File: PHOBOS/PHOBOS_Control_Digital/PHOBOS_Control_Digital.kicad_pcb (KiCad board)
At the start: 4 copper layers, 58.4 x 35.6 mm, 71 parts, among them J12 PWR, J14 PS1-2, J15 PS3-4, J2 RF_OUT, J3 USB4056-03-A_REVA2, J4 BATT, J8 BOOT, U1 SX1280IMLTRT, U2 W25Q128JVSIQ, U3 NCP1117-3.3_SOT223, U4 RP2040, U5 TPS60403DBV, Y1 C1E-52.000-10-1012-X-M, Y2 ABM8-272-T3

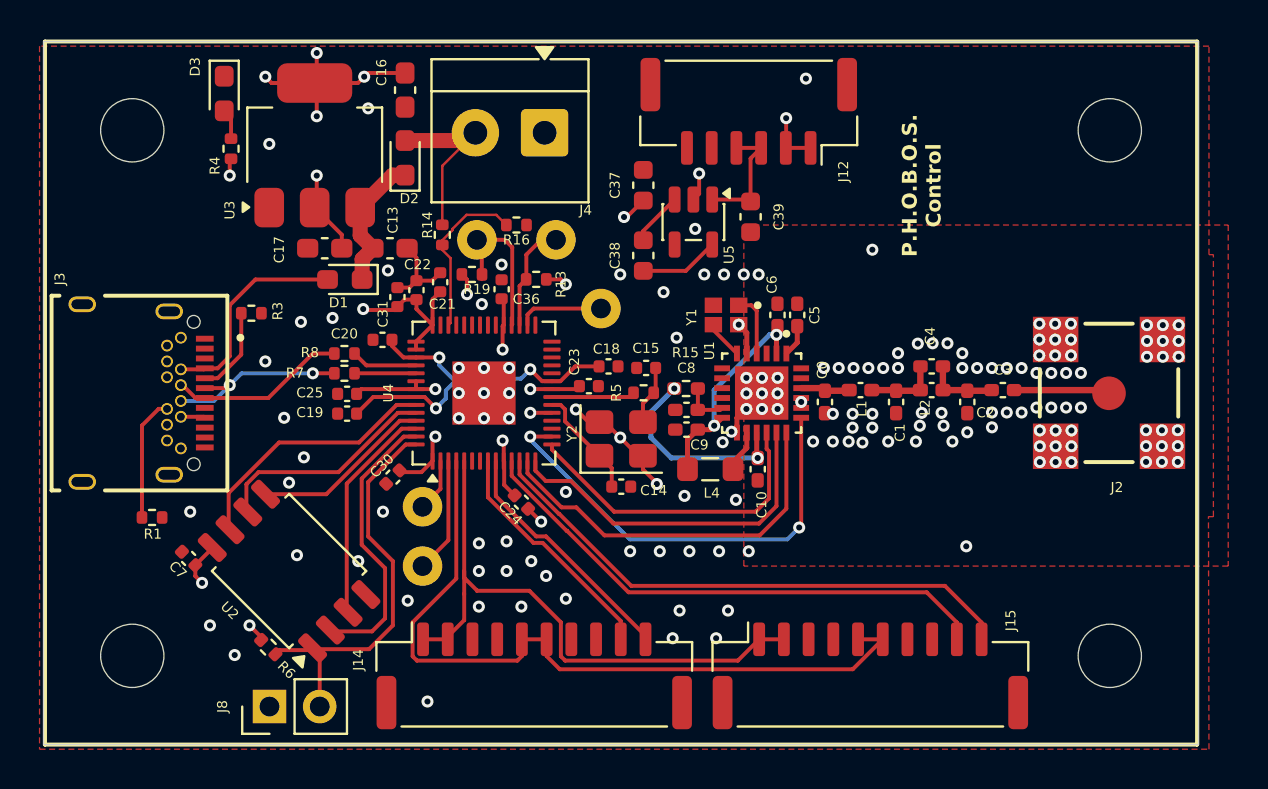
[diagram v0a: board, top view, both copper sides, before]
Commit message: DRC updates for Advanced PCB begun
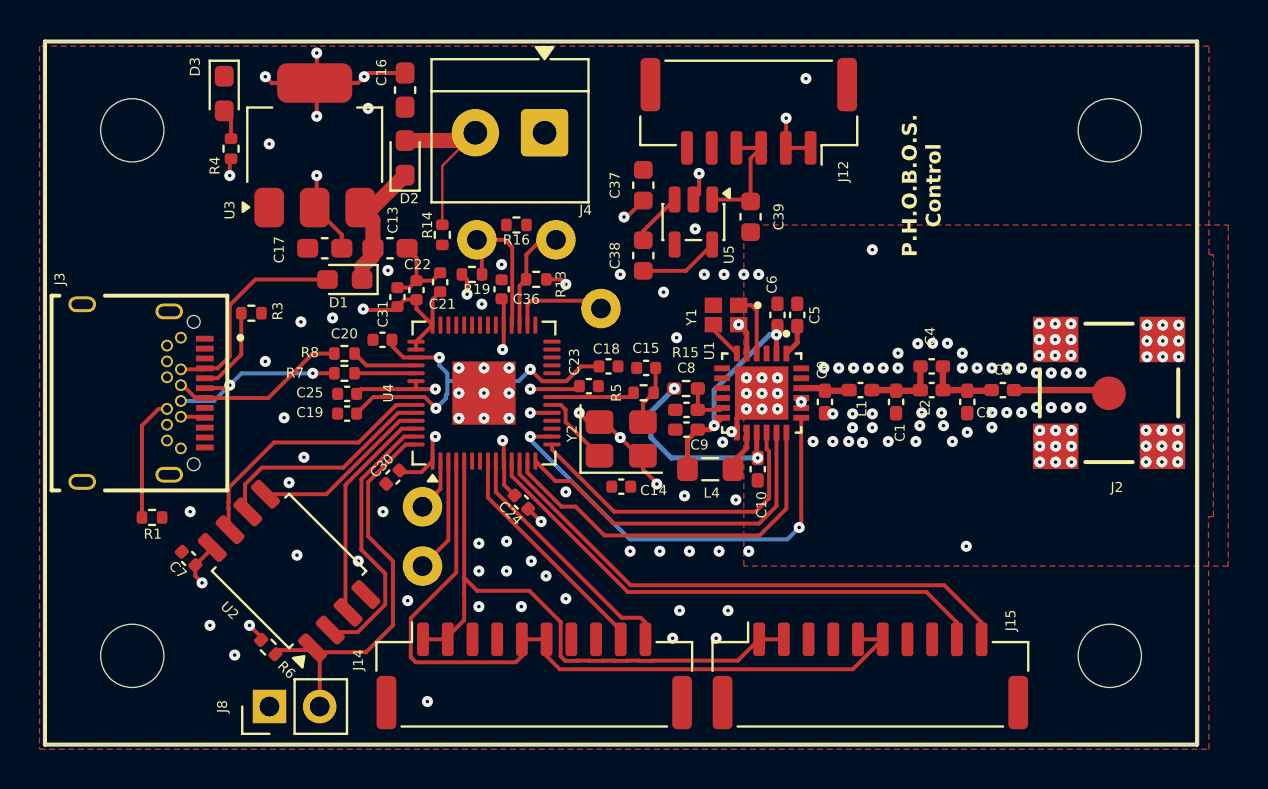
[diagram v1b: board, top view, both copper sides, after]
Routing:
- net /BATT_CONT: track 8.53 -> 0.00 mm
- net /XIN: track 5.64 -> 3.83 mm
- net +1V1: track 19.9 -> 19.0 mm
- net Net-(U4-GPIO19): track 4.37 -> 5.00 mm

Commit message: updated for Advanced PCB manufacturing capabilities. Inquire about impedance matching, also Sim
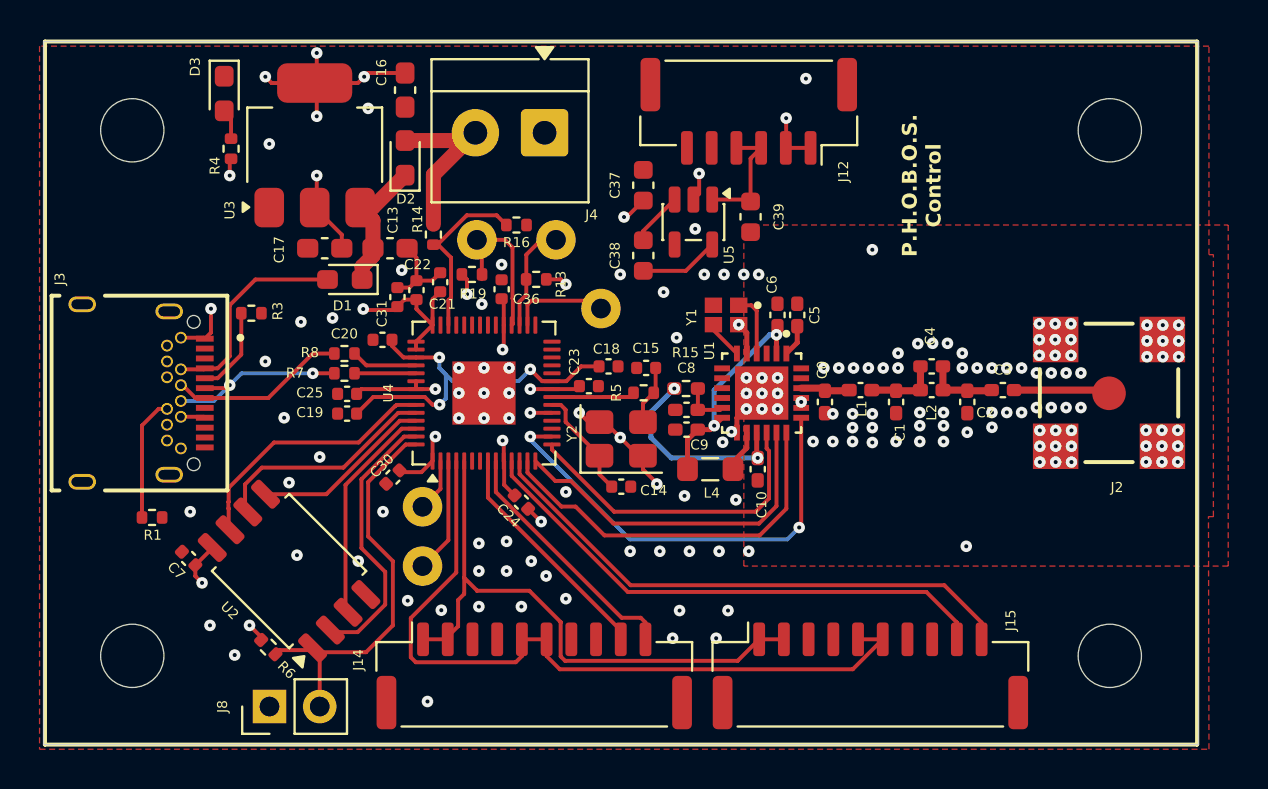
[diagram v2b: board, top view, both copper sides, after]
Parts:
- moved R14 0.45 mm to (150.1, 90.4)
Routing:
- net /BATT_CONT: track 0.00 -> 9.14 mm
- net GND: track 16.3 -> 19.2 mm, vias 159 -> 161
- net /XIN: track 3.83 -> 5.65 mm

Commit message: CPWG changed to microstrip. Trace width updated
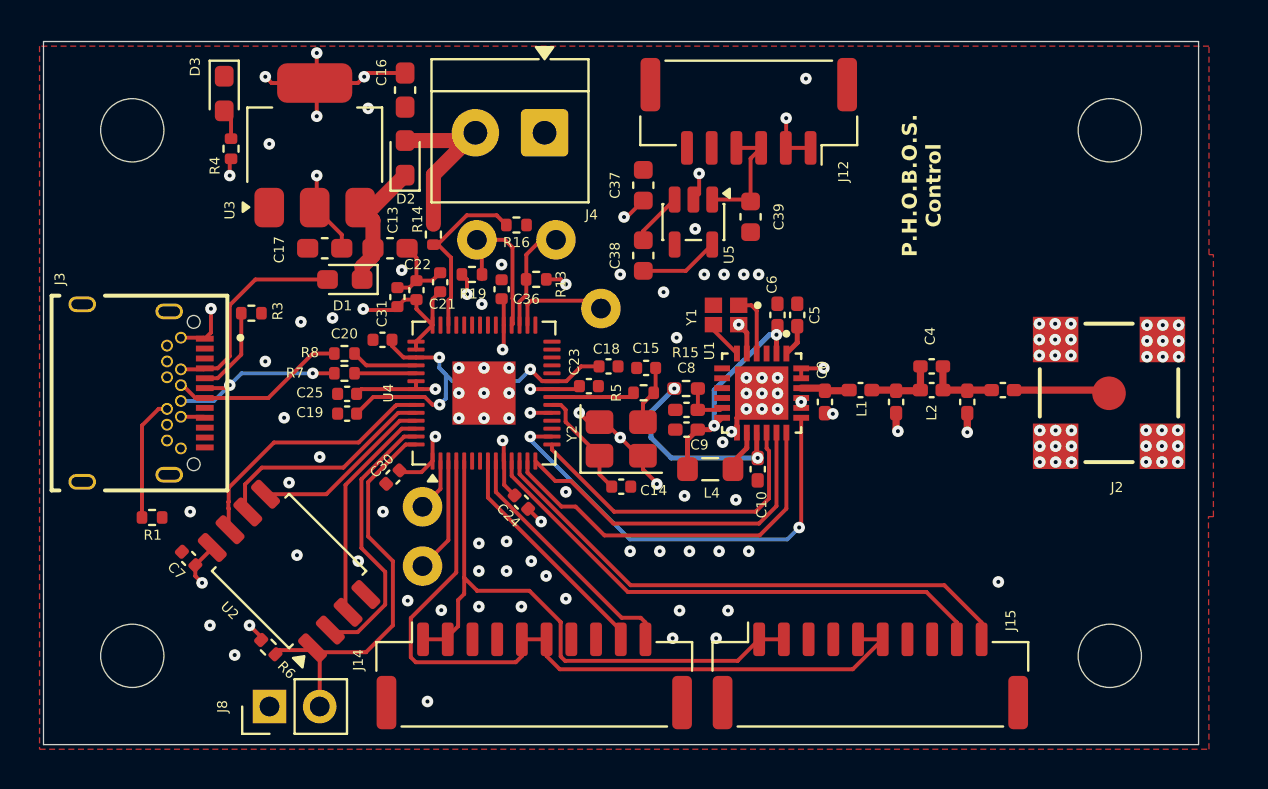
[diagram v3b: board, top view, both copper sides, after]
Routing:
- net GND: track 19.2 -> 22.8 mm, vias 161 -> 119
